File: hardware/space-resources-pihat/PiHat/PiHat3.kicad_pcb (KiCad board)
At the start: 2 copper layers, 77.9 x 62 mm, 47 parts, among them J1 GPIO, J10 Conn_01x02_Socket, J11 Conn_01x03_Socket, J12 Conn_01x03_Socket, J13 Conn_01x03_Socket, J14 Conn_01x02_Socket, J2 Conn_01x02_Socket, J3 Conn_01x04_Socket, J4 Conn_01x04_Socket, J5 Conn_01x02_Socket, J6 Conn_01x02_Socket, J7 Conn_01x02_Socket, J8 Conn_01x04_Socket, J9 Conn_01x02_Socket, M1 AO3400A, M3 AO3400A, U1 TPS54560BDDA

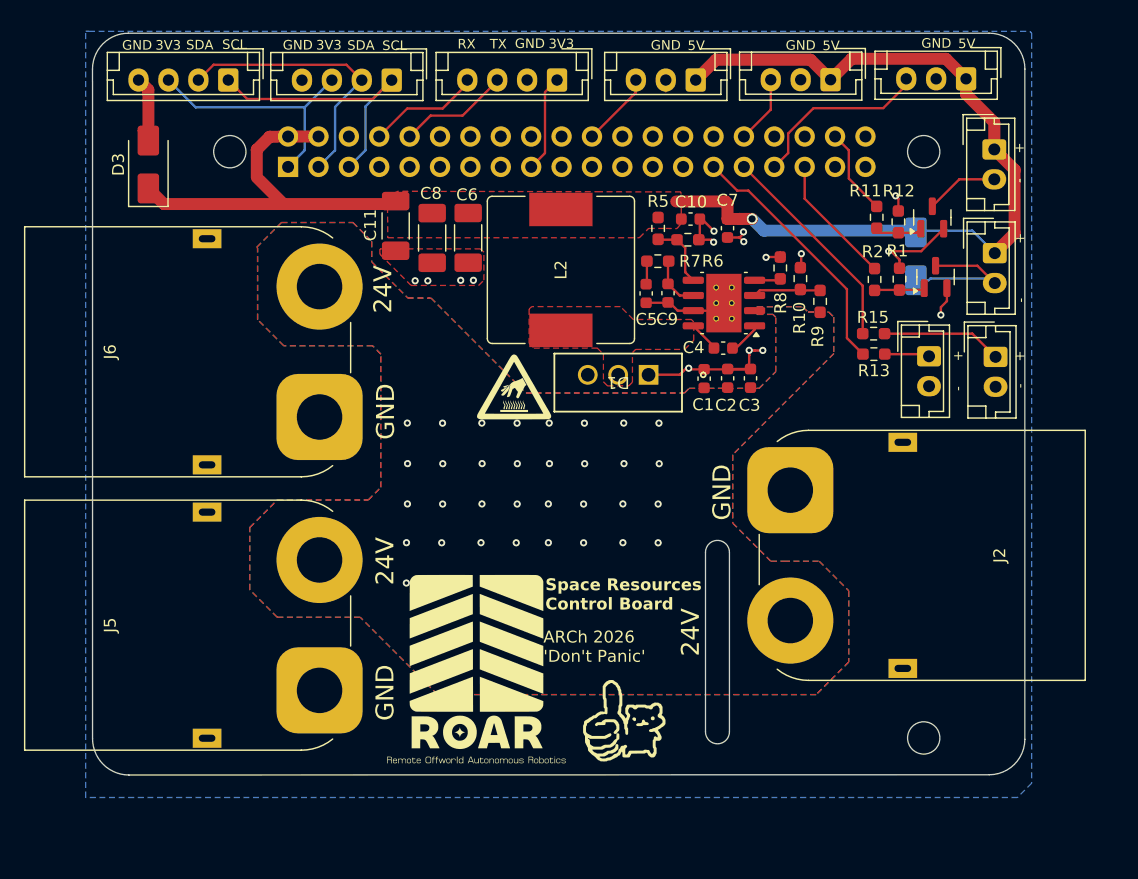
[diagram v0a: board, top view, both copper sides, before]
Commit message: fix: fixed TX/RX UART silkscreen, moved input XT90
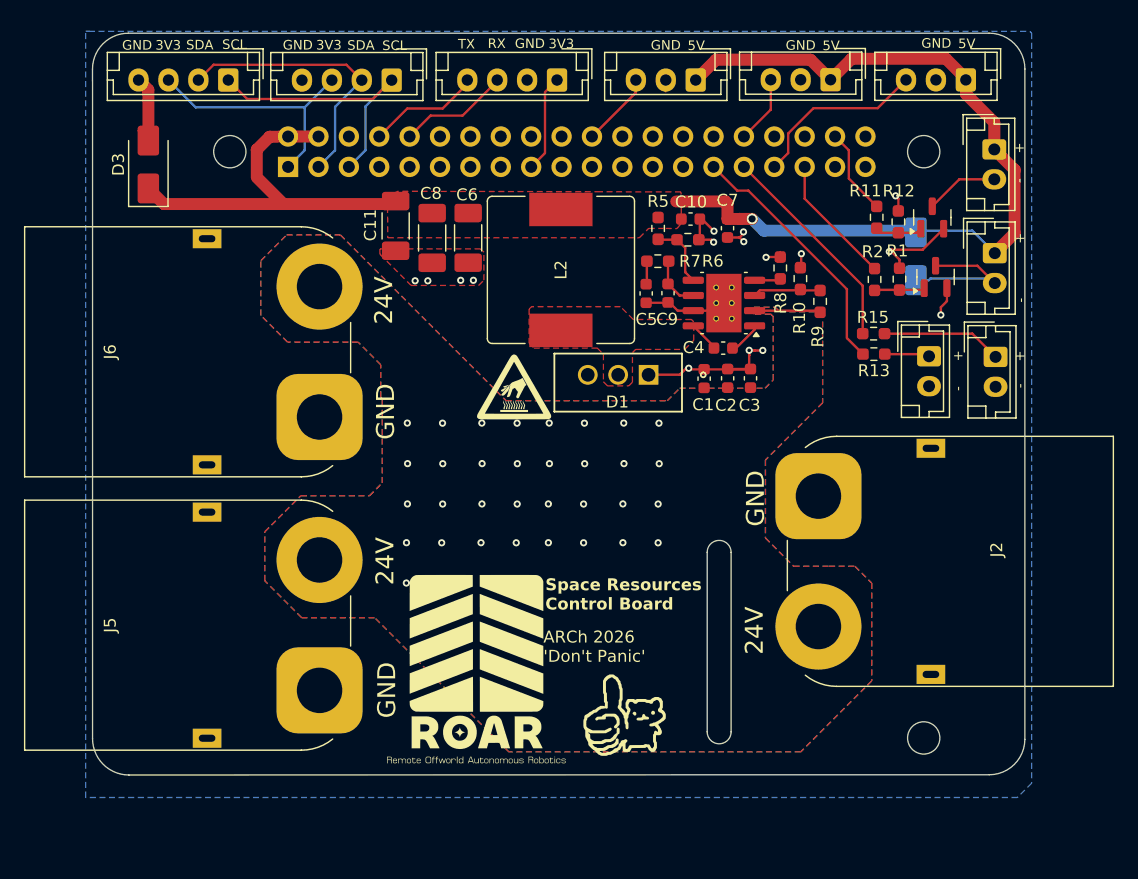
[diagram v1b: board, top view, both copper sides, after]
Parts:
- moved J2 2.40 mm to (152.7, 76.3)
- moved J13 0.09 mm to (165.0, 41.5)
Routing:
- net 24V: track 1.91 -> 7.44 mm
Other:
- outline, holes or cut-outs redrawn

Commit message: fix: Changed buck input and output caps for digikey stocked components
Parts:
- removed D3: SMAZ5V1-13-F, Diode_SMD:D_SMA
- C1, C2, C3: footprint Capacitor_SMD:C_0603_1608Metric -> Capacitor_SMD:C_1206_3216Metric_Pad1.33x1.80mm_HandSolder
- C11, C6, C8: footprint Capacitor_SMD:C_1808_4520Metric -> Capacitor_SMD:C_1210_3225Metric_Pad1.33x2.70mm_HandSolder
- moved C6 27.7 mm to (96.5, 48.3), turned to 90 degrees
- moved C8 2.03 mm to (122.4, 54.8)
- moved C11 1.71 mm to (118.8, 54.6)
- moved C1 1.62 mm to (141.7, 67.3)
- moved D1 1.44 mm to (137.1, 66.2)
- moved C2 0.96 mm to (144.7, 67.3)
- moved C3 0.89 mm to (147.3, 67.3)
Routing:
- net GND: track 49.5 -> 59.3 mm, vias 16 -> 15
- net 5V: track 104.8 -> 107.5 mm

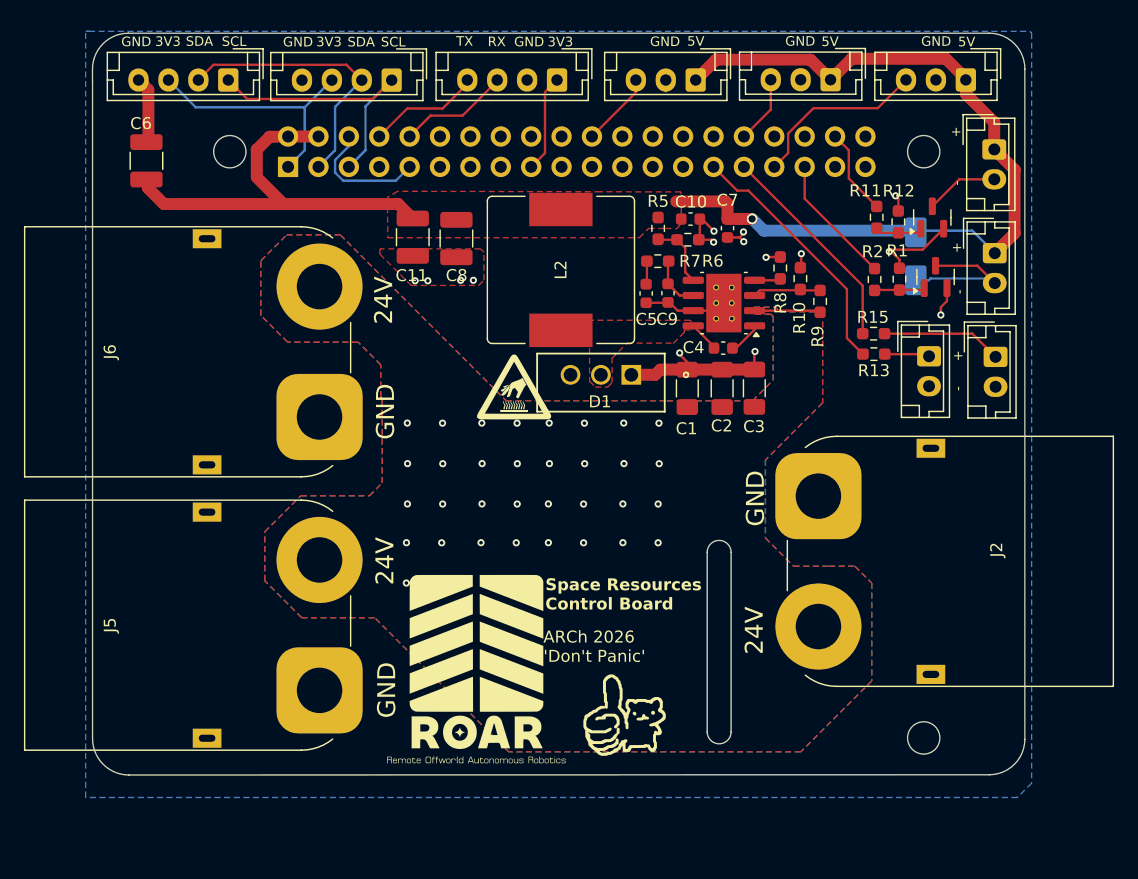
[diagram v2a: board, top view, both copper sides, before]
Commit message: fix: Rectified layout to fit properly with Pi4, added various testpoints and optional i2c pullup resistors
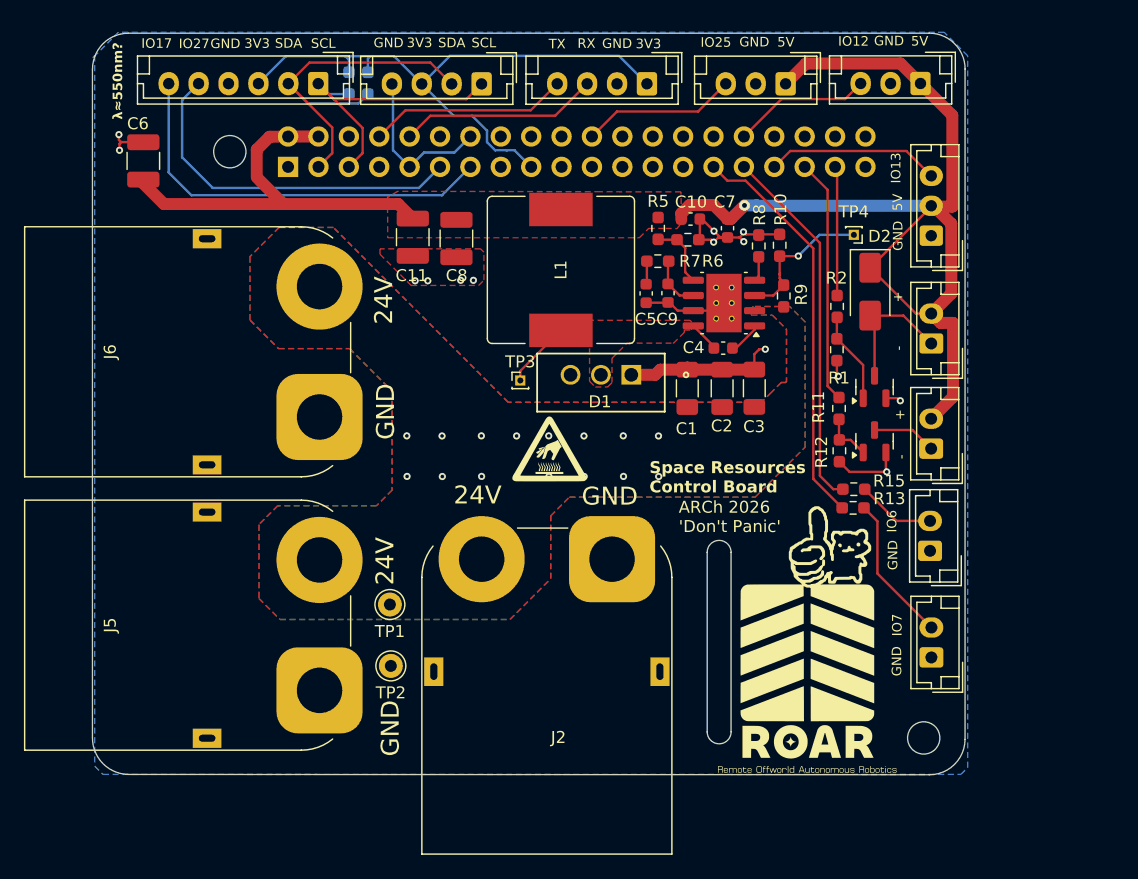
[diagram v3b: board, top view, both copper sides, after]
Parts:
- removed MH2: MountingHole_2.7mm_M2.5, MountingHole:MountingHole_2.7mm_M2.5
- added R3: 10k, Resistor_SMD:R_0603_1608Metric_Pad0.98x0.95mm_HandSolder, B.Cu at (113.5, 41.8)
- added R4: 10k, Resistor_SMD:R_0603_1608Metric_Pad0.98x0.95mm_HandSolder, B.Cu at (115.0, 41.8)
- added TP1: TestPoint, Connector_Pin:Pin_D1.0mm_L10.0mm, F.Cu at (116.9, 85.3)
- added TP2: TestPoint, Connector_Pin:Pin_D1.0mm_L10.0mm, F.Cu at (117.0, 90.5)
- added TP3: TestPoint, Connector_PinHeader_1.00mm:PinHeader_1x01_P1.00mm_Vertical, F.Cu at (127.8, 66.6)
- added TP4: TestPoint, Connector_PinHeader_1.00mm:PinHeader_1x01_P1.00mm_Vertical, F.Cu at (155.7, 54.5)
- C1, C2, C3: value 2.2u -> 10u
- D2: moved to F.Cu
- J3: value Conn_01x04_Socket -> Conn_01x06_Socket; footprint Connector_JST:JST_EH_B4B-EH-A_1x04_P2.50mm_Vertical -> Connector_JST:JST_EH_B6B-EH-A_1x06_P2.50mm_Vertical
- moved J9 25.6 mm to (162.1, 72.3), turned to 90 degrees
- moved J10 25.2 mm to (162.1, 89.8), turned to 90 degrees
- moved R12 19.8 mm to (154.4, 72.5), turned to 90 degrees
- moved M3 19.3 mm to (157.4, 71.7)
- moved J2 18.0 mm to (135.4, 81.6), turned to 180 degrees
- moved J14 17.1 mm to (162.0, 80.9), turned to 90 degrees
- moved R11 16.3 mm to (154.4, 69.0)
- moved J13 13.3 mm to (162.1, 54.5), turned to 90 degrees
- moved R15 13.1 mm to (155.7, 75.7)
- moved R13 13.0 mm to (155.6, 77.3)
- moved M1 10.5 mm to (157.4, 67.2)
- moved J7 9.23 mm to (162.1, 63.5), turned to 90 degrees
- moved R1 7.89 mm to (154.2, 64.0), turned to 90 degrees
- moved J3 7.53 mm to (110.9, 41.8)
- moved J12 7.52 mm to (150.0, 41.8)
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- renumbered L2 to L1
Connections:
- net Net-(U1-EN) renamed EN_BUCK
- net Net-(U1-SW) renamed SW
- J1 pad 11: /GPIO17 -> GPIO17
- J1 pad 13: /GPIO27 -> GPIO27
- J1 pad 37: /GPIO26 -> GPIO26
- J1 pad 38: GPIO20/PCM.DIN -> /GPIO20/PCM.DIN
- J10 pad 1: Net-(J10-Pin_1) -> GND
- J10 pad 2: GND -> Net-(J10-Pin_2)
- J13 pad 1: 5V -> GND
- J13 pad 2: GND -> 5V
- J14 pad 1: Net-(J14-Pin_1) -> GND
- J14 pad 2: GND -> Net-(J14-Pin_2)
- J7 pad 1: 5V -> Net-(D2-A)
- J7 pad 2: Net-(D2-A) -> 5V
- J9 pad 1: 5V -> Net-(J9-Pin_1)
- J9 pad 2: Net-(J9-Pin_2) -> 5V
- M3 pad 3: Net-(J9-Pin_2) -> Net-(J9-Pin_1)
- R11 pad 2: GPIO20/PCM.DIN -> GPIO19/PCM.FS
- R13 pad 1: Net-(J10-Pin_1) -> Net-(J10-Pin_2)
- R15 pad 1: Net-(J14-Pin_1) -> Net-(J14-Pin_2)
- R2 pad 2: GPIO19/PCM.FS -> GPIO26
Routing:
- net GPIO27: track 0.00 -> 34.4 mm
- net GPIO17: track 0.00 -> 30.1 mm
- net 3V3: track 29.8 -> 52.4 mm
- net 5V: track 107.5 -> 120.2 mm
- net GPIO6: track 18.2 -> 30.8 mm
- net GPIO5: track 21.4 -> 33.8 mm
- net Net-(J10-Pin_2): track 0.00 -> 12.3 mm
- net GPIO26: track 0.00 -> 10.8 mm
- net Net-(J14-Pin_1): track 10.1 -> 0.00 mm
- net GPIO19/PCM.FS: track 10.9 -> 20.5 mm
- net GPIO2/SDA1: track 23.5 -> 31.7 mm
- net GPIO14/TXD0: track 9.50 -> 17.0 mm
- net GPIO15/RXD0: track 9.26 -> 16.7 mm
- net GPIO20/PCM.DIN: track 7.28 -> 0.00 mm
- net SW: track 2.44 -> 9.48 mm
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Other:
- board size 77.9 x 62 mm -> 72.9 x 62 mm
- board text added: "IO12"
- board text added: "IO13"
- board text added: "IO17"
- board text added: "IO25"
- board text added: "IO27"
- board text added: "IO6"
- board text added: "IO7"
- board text added: "λ≈550nm?"

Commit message: fix: Final touchups, ready for order
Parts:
- added C12: 22u, Capacitor_SMD:C_1210_3225Metric_Pad1.33x2.70mm_HandSolder, F.Cu at (98.2, 48.0)
- TP1, TP2: footprint Connector_Pin:Pin_D1.0mm_L10.0mm -> Connector_PinHeader_1.00mm:PinHeader_1x01_P1.00mm_Vertical
- moved C11 25.0 mm to (94.7, 48.0), turned to 90 degrees
- moved C6 23.6 mm to (119.0, 54.7), turned to -90 degrees
- moved TP2 1.16 mm to (117.1, 89.3)
- moved R3 0.67 mm to (112.8, 41.9)
- moved TP1 0.38 mm to (117.1, 85.0)
- moved R4 0.09 mm to (115.0, 41.9)
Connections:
- R3 pad 2: Net-(R3-Pad2) -> 3V3
- R4 pad 2: Net-(R3-Pad2) -> 3V3
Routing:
- net 5V: track 120.2 -> 78.4 mm
- net GND: track 59.5 -> 69.3 mm, vias 14 -> 24
- net 3V3: track 52.4 -> 62.1 mm
- net GPIO3/SCL1: track 26.6 -> 26.0 mm
